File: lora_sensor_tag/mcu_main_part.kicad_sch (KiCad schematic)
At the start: 45 parts, among them J1 Conn_Coaxial, U1 SX1276IMLTRT, U2 ESP32-WROOM-32D, U3 PE4259, U4 SHT20, Y1 32 MHz

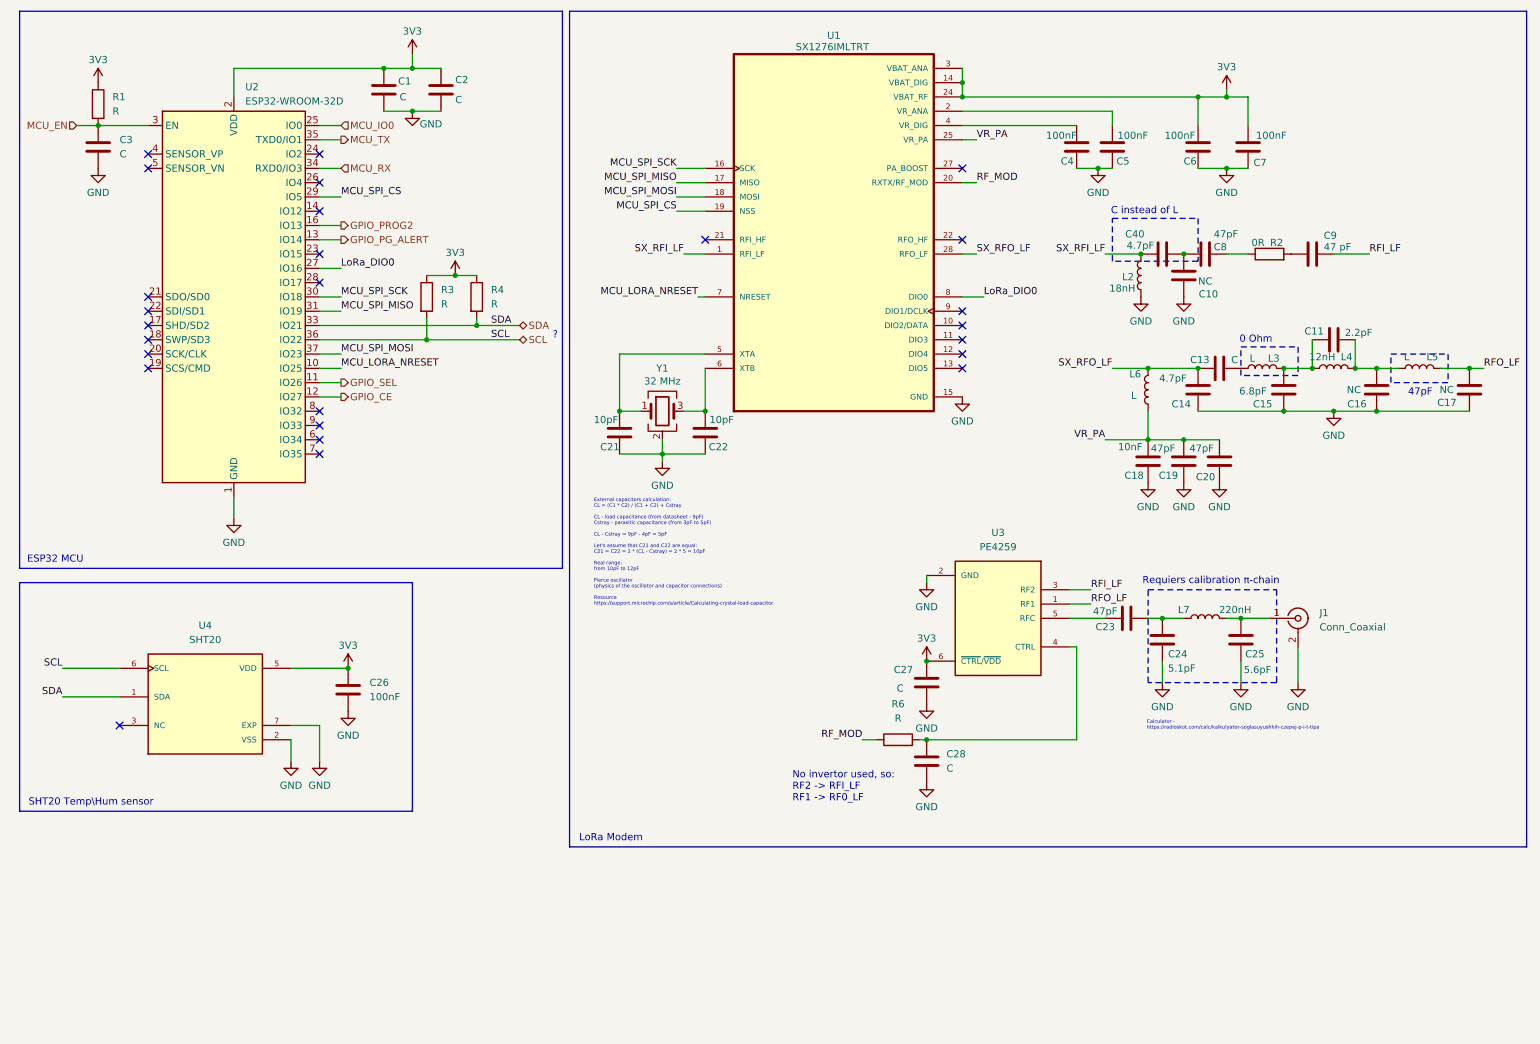
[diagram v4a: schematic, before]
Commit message: Large schematic update
This commit update the following:

 - Update MCP73871 CE control schematic
 - Finished schematic development and footprint
   assignment

Signed-off-by: Volodymyr <volodymyrnoha99@gmail.com>
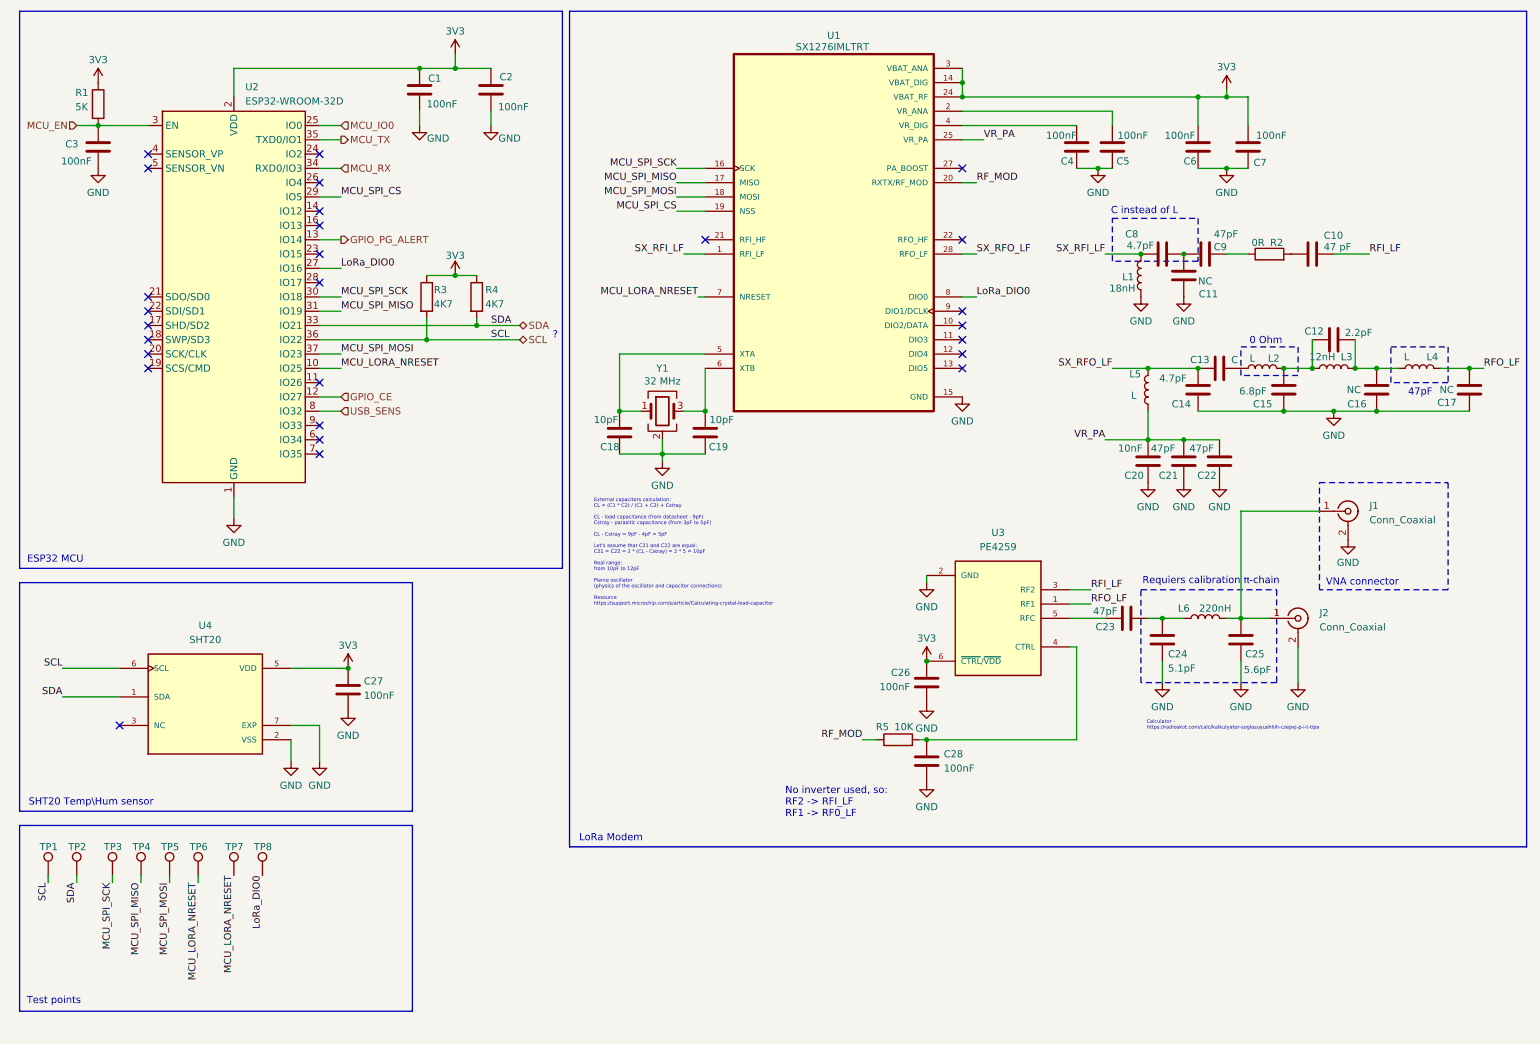
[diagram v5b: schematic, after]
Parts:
- added J1: Conn_Coaxial, Connector_Coaxial:SMA_BAT_Wireless_BWSMA-KWE-Z001, symbol Connector:Conn_Coaxial
- added TP1, TP2, TP3, TP4, TP5, TP6, TP7, TP8: TestPoint, TestPoint:TestPoint_Pad_D1.0mm, symbol Connector:TestPoint
- C1, C2, C28, C3: value C -> 100nF; footprint (none) -> Capacitor_SMD:C_0603_1608Metric
- C10: renamed from C9; footprint (none) -> Capacitor_SMD:C_0402_1005Metric
- C11: renamed from C10; footprint (none) -> Capacitor_SMD:C_0402_1005Metric
- C12: renamed from C11; footprint (none) -> Capacitor_SMD:C_0402_1005Metric
- C13, C14, C15, C16, C17, C23, C24, C25: footprint (none) -> Capacitor_SMD:C_0402_1005Metric
- C18: renamed from C21; footprint (none) -> Capacitor_SMD:C_0603_1608Metric
- C19: renamed from C22; footprint (none) -> Capacitor_SMD:C_0603_1608Metric
- C20: renamed from C18; footprint (none) -> Capacitor_SMD:C_0402_1005Metric
- C21: renamed from C19; footprint (none) -> Capacitor_SMD:C_0402_1005Metric
- C22: renamed from C20; footprint (none) -> Capacitor_SMD:C_0402_1005Metric
- C26: renamed from C27; value C -> 100nF; footprint (none) -> Capacitor_SMD:C_0603_1608Metric
- C27: renamed from C26; footprint (none) -> Capacitor_SMD:C_0603_1608Metric
- C4, C5, C6, C7: footprint (none) -> Capacitor_SMD:C_0603_1608Metric
- C8: renamed from C40; footprint (none) -> Capacitor_SMD:C_0402_1005Metric
- C9: renamed from C8; footprint (none) -> Capacitor_SMD:C_0402_1005Metric
- L1: renamed from L2; footprint Relay_THT:Relay_DPDT_Finder_30.22 -> Inductor_SMD:L_0402_1005Metric
- L2: renamed from L3; footprint Relay_THT:Relay_DPDT_Finder_30.22 -> Resistor_SMD:R_0402_1005Metric
- L3: renamed from L4; footprint Relay_THT:Relay_DPDT_Finder_30.22 -> Inductor_SMD:L_0402_1005Metric
- L4: renamed from L5; footprint Relay_THT:Relay_DPDT_Finder_30.22 -> Capacitor_SMD:C_0402_1005Metric
- L5: renamed from L6; footprint Relay_THT:Relay_DPDT_Finder_30.22 -> Inductor_SMD:L_0402_1005Metric
- L6: renamed from L7; footprint Relay_THT:Relay_DPDT_Finder_30.22 -> Inductor_SMD:L_0402_1005Metric
- R1: value R -> 5K; footprint TPS63070RNMR:VREG_TPS63070RNMR -> Resistor_SMD:R_0603_1608Metric
- R3, R4: value R -> 4K7; footprint TPS63070RNMR:VREG_TPS63070RNMR -> Resistor_SMD:R_0603_1608Metric
- R5: renamed from R6; value R -> 10K; footprint TPS63070RNMR:VREG_TPS63070RNMR -> Resistor_SMD:R_0603_1608Metric
- Y1: footprint (none) -> Crystal:Crystal_SMD_3225-4Pin_3.2x2.5mm
- renumbered J1 to J2
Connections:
- net GND: now also J1.2 (Ext)
- net LoRa_DIO0: now also TP8.1
- net MCU_LORA_NRESET: now also TP6.1, TP7.1
- net MCU_SPI_MISO: now also TP4.1
- net MCU_SPI_MOSI: now also TP5.1
- net MCU_SPI_SCK: now also TP3.1
- net SCL: now also TP1.1
- net SDA: now also TP2.1
- net at C25.2, J2.1 (In), L6.2: now also J1.1 (In)
- net USB_SENS: now reaches U2.8 (IO32)
- net GPIO_PROG2: no longer names the net of U2.16 (IO13)
- net GPIO_SEL: no longer names the net of U2.11 (IO26)
- no-connect marks 26 -> 27
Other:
- note added: "No inverter used, so: RF2 -> RFI_LF RF1 -> RF0_LF"
- note added: "Test points"
- note added: "VNA connector"
- note removed: "No invertor used, so: RF2 -> RFI_LF RF1 -> RF0_LF"
- moved on the sheet: C1, C2

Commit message: Update schematics
Adds the following updates to the schematics:
- Add power switch to the device;
- Add various LED indicators for device status monitoring;
- Add Reset and Prog buttons for device control;

Signed-off-by: Volodymyr <volodymyrnoha99@gmail.com>
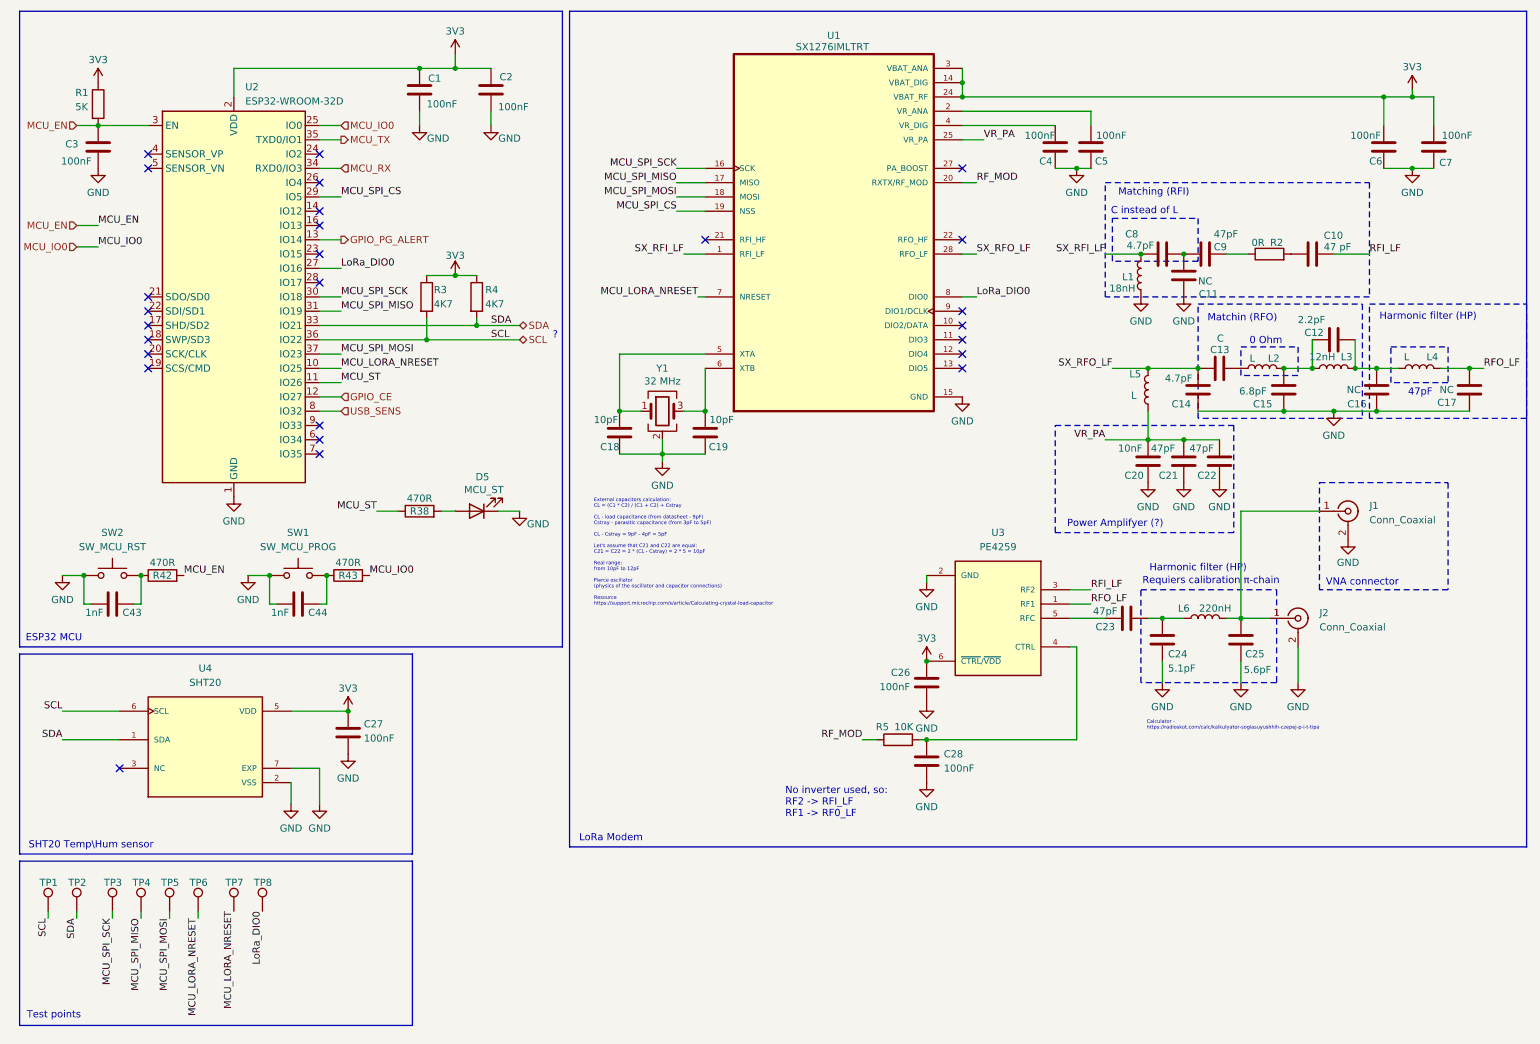
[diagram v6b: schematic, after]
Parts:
- added C43, C44: 1nF, Capacitor_SMD:C_0603_1608Metric, symbol Device:C
- added D5: MCU_ST, LED_SMD:LED_0603_1608Metrica, symbol Device:LED
- added R38, R42, R43: 470R, Resistor_SMD:R_0603_1608Metric, symbol Device:R
- added SW1: SW_MCU_PROG, Button_Switch_SMD:SW_Push_1TS009xxxx-xxxx-xxxx_6x6x5mm, symbol Switch:SW_Push
- added SW2: SW_MCU_RST, Button_Switch_SMD:SW_Push_1TS009xxxx-xxxx-xxxx_6x6x5mm, symbol Switch:SW_Push
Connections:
- net GND: now also C43.1, C44.1, D5.1 (K), SW1.1, SW2.1
- net MCU_EN: now also R42.2
- net MCU_IO0: now also R43.2
- net MCU_ST: now reaches U2.11 (IO26)
- net MCU_ST: now also R38.1
- new net: C44.2, R43.1, SW1.2
- new net: C43.2, R42.1, SW2.2
- new net: D5.2 (A), R38.2
- no-connect marks 27 -> 26
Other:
- note added: "Harmonic filter (HP)"
- note added: "Matchin (RFO)"
- note added: "Matching (RFI)"
- note added: "Power Amplifyer (?)"
- moved on the sheet: C27, C4, C5, C6, C7, TP1, TP2, TP3, TP4, TP5, TP6, TP7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

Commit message: pcb_layout: Add initial board layout
Adds:
 - Initial board dimensions;
 - Initial MCU component placement and routing

Signed-off-by: Volodymyr <volodymyrnoha99@gmail.com>
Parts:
- added H1, H2, H3, H4: MountingHole_Pad, MountingHole:MountingHole_2.7mm_M2.5_Pad_Via, symbol Mechanical:MountingHole_Pad
- D1: renamed from D5; footprint LED_SMD:LED_0603_1608Metrica -> LED_SMD:LED_0603_1608Metric
- R2: footprint TPS63070RNMR:VREG_TPS63070RNMR -> Resistor_SMD:R_0603_1608Metric
- renumbered C43 to C23, C44 to C24, C23 to C25, C24 to C26, C25 to C27, C26 to C28, C27 to C29, C28 to C30, R38 to R5, R42 to R6, R43 to R7, R5 to R8, SW2 to SW1, SW1 to SW2
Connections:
- net GND: now also H1.1, H2.1, H3.1, H4.1

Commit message: Update PCB layout routing
Updates and adds the following changes to the PCB
layout routing:
- Changed board dimensions and topology;
- Add layout for MCP73871 Li-ion battery charger;
- Add layout for MAX17048 Fuel Gauge;

Signed-off-by: Volodymyr <volodymyrnoha99@gmail.com>
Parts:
- removed H1, H2, H3, H4: MountingHole_Pad, MountingHole:MountingHole_2.7mm_M2.5_Pad_Via, symbol Mechanical:MountingHole_Pad
- added R46: 0R, Resistor_SMD:R_0402_1005Metric, symbol Device:R
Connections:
- net at C27.2, J2.1 (In), L6.2: now also R46.1; no longer J1.1 (In)
- new net: J1.1 (In), R46.2
